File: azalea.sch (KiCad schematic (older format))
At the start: 103 parts, among them J1 NEIGHBOR1, J2 NEIGHBOR2, J3 USB-MICRO-B-SHIELDED, J4 USB-MICRO-B-SHIELDED, J5 JTAG, J6 POWER, J7 BONUS_ROW, SW1 DFU, SW2 RESET, U1 LPC4330FBD144, U2 W25Q16DV, U3 AP7333, U4 IP4220CZ6, U5 AP2553W6-7, X1 MCU_XTAL, X2 RTC_XTAL

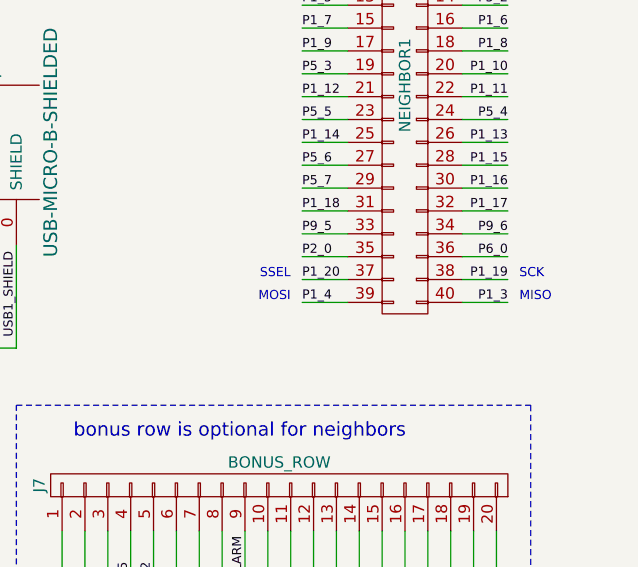
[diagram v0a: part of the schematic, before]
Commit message: adopt OSHWA convention for SPI signal names https://www.oshwa.org/a-resolution-to-redefine-spi-signal-names
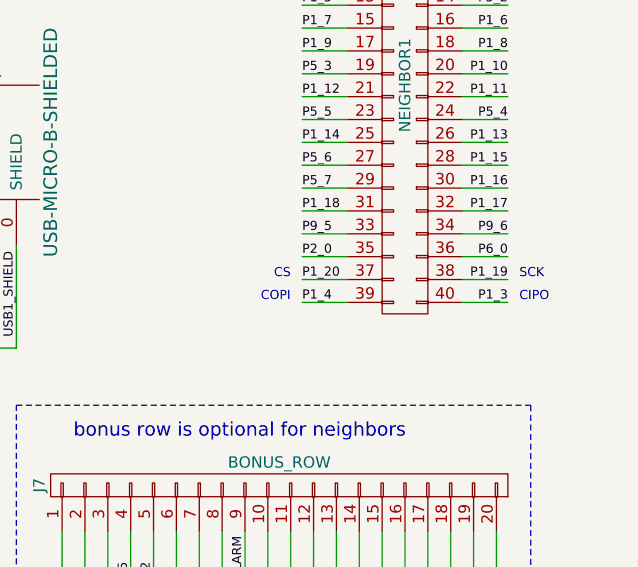
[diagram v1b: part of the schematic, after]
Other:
- note added: "CIPO"
- note added: "COPI"
- note added: "CS"
- note removed: "MISO"
- note removed: "MOSI"
- note removed: "SSEL"
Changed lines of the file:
@@
 P2_0
 Text Notes 16250 6200 0    40   ~ 0
-MISO
+CIPO
 Text Notes 15250 6200 2    40   ~ 0
-MOSI
+COPI
 Text Notes 16250 6100 0    40   ~ 0
 SCK
 Text Notes 15250 6100 2    40   ~ 0
-SSEL
+CS
 Text Label 16300 3600 2    40   ~ 0
 I2C0_SCL

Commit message: GF1 Hardware: Update schematic for modern KiCAD
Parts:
- C1, C10, C11, C12, C13, C14, C15, C16, C17, C18, C19, C2, C20, C21, C22, C23, C24, C25, C3, C4, C5, C6, C7, C8, C9: symbol C -> Device:C
- D1, D2, D3, D4: symbol LED -> Device:LED
- D5: symbol D -> Device:D
- FB1, FB2, FB3: symbol FILTER -> Device:Ferrite_Bead
- J1, J2: symbol CONN_02X20 -> Connector_Generic:Conn_02x20_Odd_Even
- J3, J4: symbol USB-MICRO-B-SHIELDED -> gsg-symbols:USB-MICRO-B-SHIELDED
- J5: symbol CONN_02X05 -> Connector_Generic:Conn_02x05_Odd_Even
- J6: symbol CONN_02X04 -> Connector_Generic:Conn_02x04_Odd_Even
- J7: symbol CONN_01X20 -> Connector_Generic:Conn_01x20
- MH1, MH2, MH3, MH4, TP1, TP10, TP11, TP12, TP13, TP14, TP15, TP16, TP17, TP18, TP19, TP2, TP3, TP4, TP5, TP6, TP7, TP8, TP9: symbol CONN_01X01 -> Connector_Generic:Conn_01x01
- R1, R10, R11, R12, R13, R14, R15, R16, R17, R18, R19, R2, R20, R21, R22, R23, R24, R25, R26, R27, R28, R29, R3, R30, R4, R5, R6, R7, R8, R9: symbol R -> Device:R
- SW1, SW2: symbol SW_PUSH -> Switch:SW_Push
- U1: symbol LPC43XXFBD144 -> gsg-symbols:LPC43XXFBD144
- U2: symbol W25Q80BV -> gsg-symbols:W25Q80BV
- U3: symbol AP7333 -> gsg-symbols:AP7333
- U4: symbol IP4220CZ6 -> gsg-symbols:IP4220CZ6
- U5: symbol NX5P2553GV -> gsg-symbols:NX5P2553GV
- W1: symbol TEST_2P -> Connector:TestPoint_2Pole
- X1: symbol XTAL4PIN -> gsg-symbols:XTAL4PIN
- X2: symbol Crystal -> Device:Crystal
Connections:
- net GND: now also FB2.2, FB3.1; no longer FB2.1, FB3.2
- net USB0_SHIELD: now also FB2.1; no longer FB2.2
- net USB0_VBUS: now also FB1.2; no longer FB1.1
- net USB1_SHIELD: now also FB3.2; no longer FB3.1
- net at D5.2 (A), R25.1, W1.2: now also FB1.1; no longer FB1.2
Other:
- moved on the sheet: SW1, SW2
